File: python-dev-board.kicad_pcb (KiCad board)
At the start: 2 copper layers, 38 parts, among them IC1 STM32F405RGT, J2 503182-1852, J3 USB_OTG, SW1 SW_Push, U1 LT1521-3.3, Y1 8MHz, Y2 32.768KHz

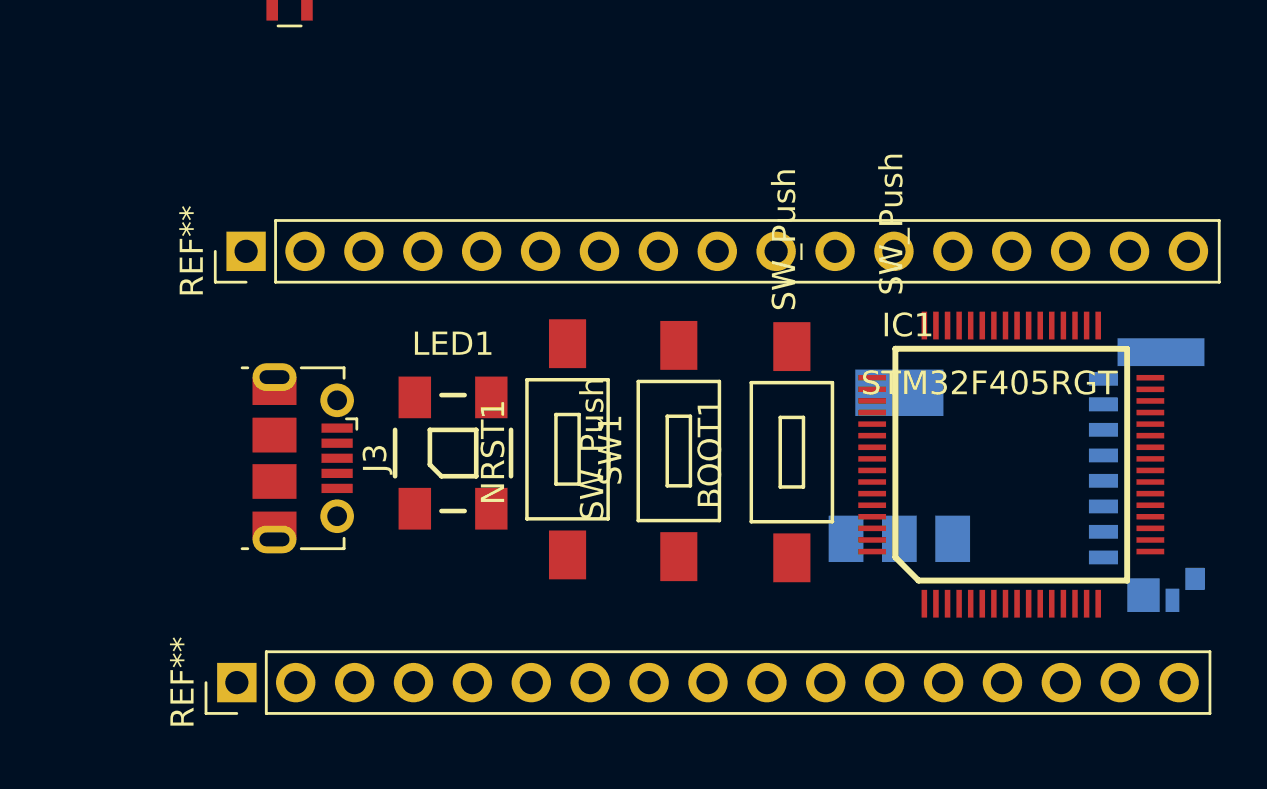
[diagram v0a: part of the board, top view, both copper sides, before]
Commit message: added pin headers to schematic
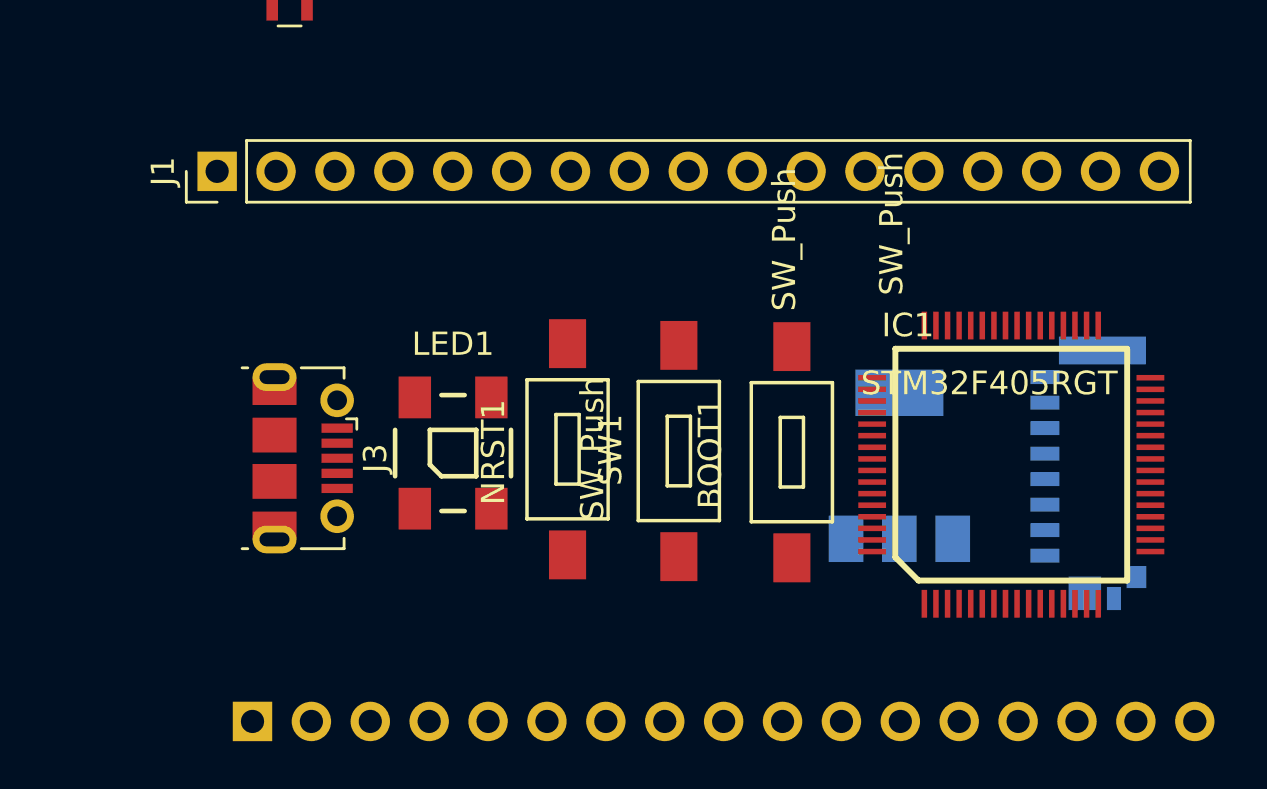
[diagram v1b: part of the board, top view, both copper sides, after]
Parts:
- removed REF** (x2): Pin_Header_Straight_1x17_Pitch2.54mm, Pin_Headers:Pin_Header_Straight_1x17_Pitch2.54mm
- added J1: Conn_01x17, Pin_Headers:Pin_Header_Straight_1x17_Pitch2.54mm, F.Cu at (141.1, 85.8)
- added J4: 47309-2851, my_footprints:molex_sd_47309-2851, B.Cu at (176.8, 98.5)
- J2: value 503182-1852 -> Conn_01x17; footprint my_footprints:molex_sd_47309-2851 -> Pin_Headers:Pin_Header_Straight_1x17_Pitch2.54mm
- U1: value LT1521-3.3 -> LM1117-3.3
- moved J2 38.3 mm to (142.6, 109.5)
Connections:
- U1 pad 1: +BATT -> GND
- U1 pad 2: GND -> +3V3
- U1 pad 3: +3V3 -> +BATT
